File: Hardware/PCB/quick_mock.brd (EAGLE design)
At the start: 101.6 x 98.8 mm, 27 parts

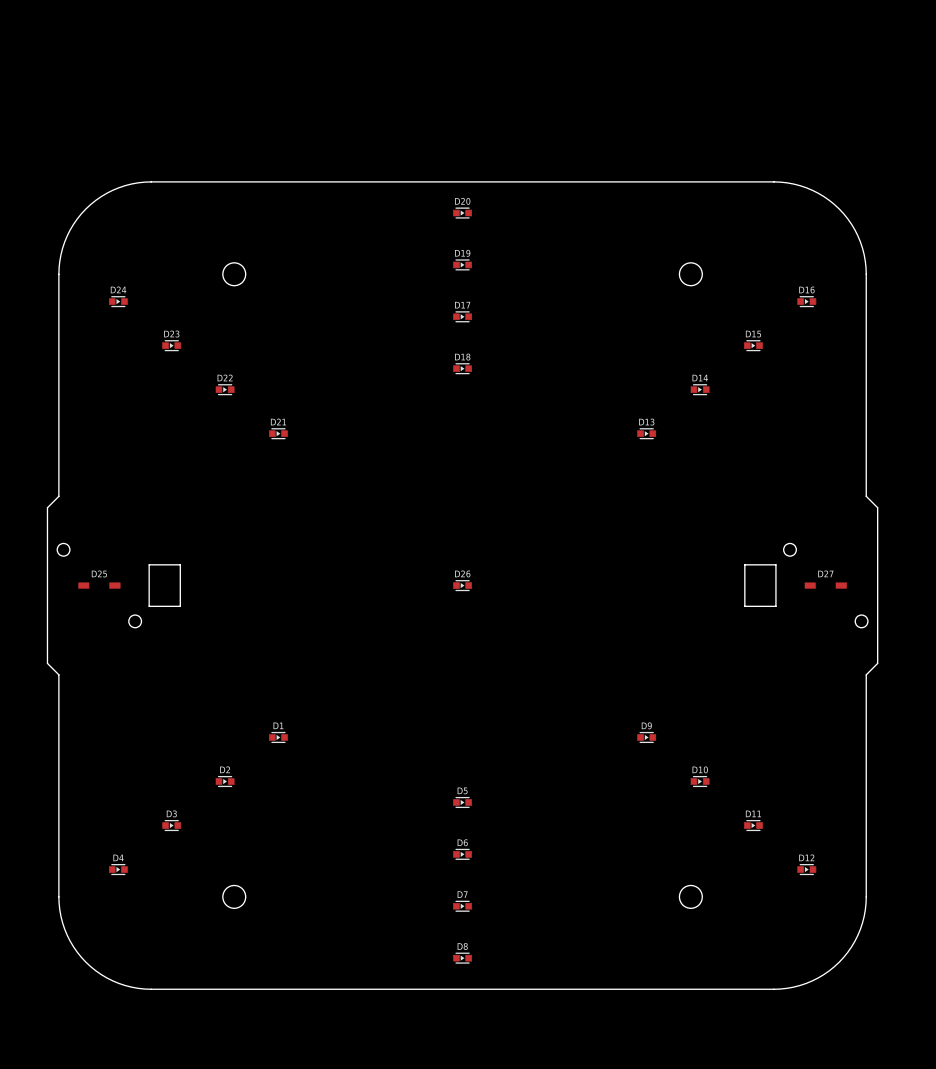
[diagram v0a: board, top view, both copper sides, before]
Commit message: move switches. add two types of lanyard mounting
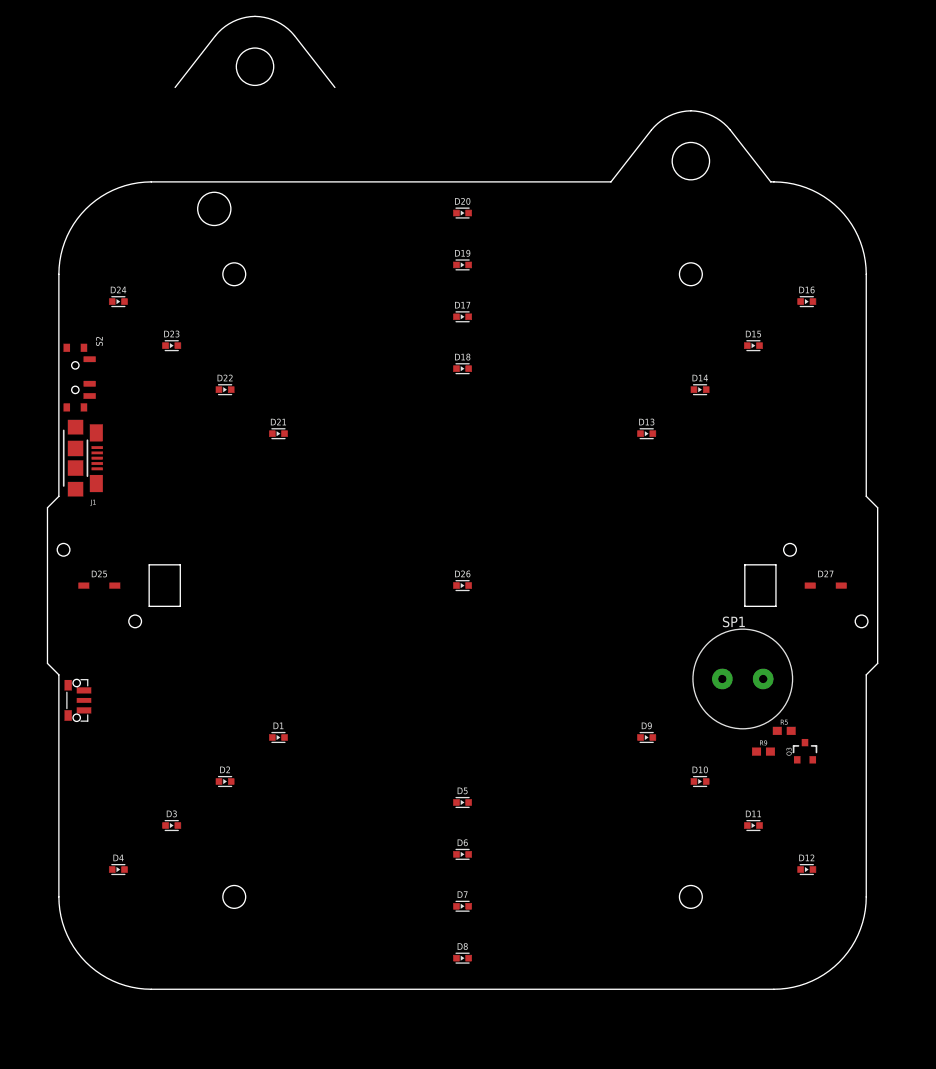
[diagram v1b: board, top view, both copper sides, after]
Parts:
- added J1: (no value), SparkFun-Connectors-new:USB-MICROB-10118192
- added Q3: 600mA/40V, SparkFun-DiscreteSemi:SOT23-3
- added R5, R9: 1k, SparkFun-Resistors:0603
- added S1: TL3340AF160QG, Rob-Switches:3PIN_GULLWING_4.0X3.3MM
- added S2: CUS-12B, IDEO-Switches:CUS-12_SPDT
- added SP1: SPEAKER/PS12, adafruit:PS12
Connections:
- new net 3.3V: R5.1, SP1.P$1
- new net BUZZER_OUT: R9.2
- new net GND: J1.GND, Q3.2
- new net N$26: Q3.1, R9.1
- new net N$3: Q3.3, R5.2, SP1.P$2
- new net VBUS: J1.VBUS
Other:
- board size 101.6 x 98.8 mm -> 101.6 x 119.1 mm
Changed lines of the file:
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@@
 <setting verticaltext="up"/>
 </settings>
-<grid distance="50" unitdist="mil" unit="mm" style="lines" multiple="1" display="yes" altdistance="5" altunitdist="mil" altunit="mil"/>
+<grid distance="50" unitdist="mil" unit="inch" style="lines" multiple="1" display="yes" altdistance="5" altunitdist="mil" altunit="mil"/>
 <layers>
 <layer number="1" name="Top" color="4" fill="1" visible="yes" active="yes"/>
@@
 <layer number="115" name="ReferenceISLANDS" color="7" fill="1" visible="no" active="yes"/>
 <layer number="116" name="Patch_BOT" color="9" fill="4" visible="no" active="yes"/>
+<layer number="117" name="art" color="7" fill="1" visible="yes" active="yes"/>
 <layer number="118" name="Rect_Pads" color="7" fill="1" visible="no" active="yes"/>
+<layer number="119" name="Bot_pads" color="1" fill="1" visible="yes" active="yes"/>
+<layer number="120" name="art2" color="7" fill="1" visible="yes" active="yes"/>
 <layer number="121" name="_tsilk" color="7" fill="1" visible="no" active="yes"/>
 <layer number="122" name="_bsilk" color="7" fill="1" visible="no" active="yes"/>
@@
 <layer number="128" name="_bValues" color="7" fill="1" visible="no" active="yes"/>
 <layer number="129" name="Mask" color="7" fill="1" visible="no" active="yes"/>
+<layer number="130" name="art3" color="7" fill="1" visible="yes" active="yes"/>
 <layer number="131" name="tAdjust" color="7" fill="1" visible="no" active="yes"/>
 <layer number="132" name="bAdjust" color="7" fill="1" visible="no" active="yes"/>
@@
 <layer number="230" name="230bmp" color="7" fill="1" visible="no" active="yes"/>
 <layer number="231" name="231bmp" color="7" fill="1" visible="no" active="yes"/>
+<layer number="232" name="Eagle3D_PG2" color="7" fill="1" visible="no" active="no"/>
+<layer number="233" name="Eagle3D_PG3" color="7" fill="1" visible="no" active="no"/>
 <layer number="248" name="Housing" color="7" fill="1" visible="no" active="yes"/>
 <layer number="249" name="Edge" color="7" fill="1" visible="no" active="yes"/>
@@
 </layers>
 <board>
-<fusionsync huburn="a.YnVzaW5lc3M6c3VuZGJlcmdmZXJhcg" projecturn="a.YnVzaW5lc3M6c3VuZGJlcmdmZXJhciMyMDIyMDkwNjU1MzEzMzI4MQ" f3durn="urn:adsk.wipprod:dm.lineage:_LBjbpjSReejQ1QNtJxQtQ" pcbguid="" lastpulledtime="" lastsyncedchangeguid="" latestrevisionid="c8c15753-8cb0-4c92-aaa7-c8cb3c30b25e" lastsyncedrevisionid="c8c15753-8cb0-4c92-aaa7-c8cb3c30b25e" lastboardhashguid="f6b63956-15fd-f67c-a3b4-4bf64a7ab889" lastpushedtime="2023-03-03T02:30:11Z" linktopcb3d="true"/>
+<fusionsync huburn="a.YnVzaW5lc3M6c3VuZGJlcmdmZXJhcg" projecturn="a.YnVzaW5lc3M6c3VuZGJlcmdmZXJhciMyMDIyMDkwNjU1MzEzMzI4MQ" f3durn="urn:adsk.wipprod:dm.lineage:_LBjbpjSReejQ1QNtJxQtQ" pcbguid="" lastpulledtime="" lastsyncedchangeguid="" latestrevisionid="f9e391af-d23a-44e8-a3fd-33513ed03db4" lastsyncedrevisionid="f9e391af-d23a-44e8-a3fd-33513ed03db4" lastboardhashguid="249d9e56-efed-2492-9fc4-1292afa326ac" lastpushedtime="2023-03-11T19:28:37Z" linktopcb3d="true"/>
 <plain>
 <wire x1="53.975" y1="24.695375" x2="53.88615625" y2="25.113003125" width="0" layer="49"/>
@@
 <circle x="12.7" y="12.7" radius="11.43" width="0.0254" layer="49"/>
 <wire x1="1.397" y1="88.9" x2="12.7" y2="100.203" width="0.0254" layer="20" curve="-90"/>
-<wire x1="12.7" y1="100.203" x2="88.9" y2="100.203" width="0.0254" layer="20"/>
 <wire x1="88.9" y1="100.203" x2="100.203" y2="88.9" width="0.0254" layer="20" curve="-90"/>
 <wire x1="100.203" y1="88.9" x2="100.203" y2="61.722" width="0.0254" layer="20"/>
@@
 <text x="97.79" y="57.15" size="1.778" layer="51" font="vector">Transmitter</text>
 <polygon width="0.1" layer="39">
-<vertex x="1.27" y="64.262"/>
-<vertex x="1.27" y="62.865"/>
-<vertex x="2.54" y="62.23"/>
-<vertex x="2.54" y="63.754"/>
-<vertex x="1.27" y="64.389"/>
-</polygon>
-<polygon width="0.1" layer="39">
-<vertex x="1.27" y="37.338"/>
-<vertex x="1.27" y="38.735"/>
-<vertex x="2.54" y="39.37"/>
-<vertex x="2.54" y="37.846"/>
-<vertex x="1.27" y="37.211"/>
-</polygon>
-<polygon width="0.1" layer="39">
 <vertex x="100.33" y="62.865"/>
 <vertex x="100.33" y="64.389"/>
@@
 <vertex x="2.54" y="82.55"/>
 </polygon>
+<hole x="20.414" y="96.901" drill="4.064"/>
+<hole x="78.74" y="102.743" drill="4.572"/>
+<wire x1="78.74" y1="108.9025" x2="73.914" y2="106.553" width="0.0254" layer="20" curve="50"/>
+<wire x1="73.914" y1="106.553" x2="68.961" y2="100.203" width="0.0254" layer="20"/>
+<wire x1="78.74" y1="108.9025" x2="83.566" y2="106.553" width="0.0254" layer="20" curve="-50"/>
+<wire x1="83.566" y1="106.553" x2="88.519" y2="100.203" width="0.0254" layer="20"/>
+<hole x="25.4" y="114.3" drill="4.572"/>
+<wire x1="25.4" y1="120.4595" x2="20.574" y2="118.11" width="0.01" layer="20" curve="50"/>
+<wire x1="20.574" y1="118.11" x2="15.621" y2="111.76" width="0.01" layer="20"/>
+<wire x1="25.4" y1="120.4595" x2="30.226" y2="118.11" width="0.01" layer="20" curve="-50"/>
+<wire x1="30.226" y1="118.11" x2="35.179" y2="111.76" width="0.01" layer="20"/>
+<wire x1="88.9" y1="100.203" x2="88.519" y2="100.203" width="0.0254" layer="20"/>
+<wire x1="68.961" y1="100.203" x2="12.7" y2="100.203" width="0.0254" layer="20"/>
 </plain>
 <attributes>
@@
 <attribute name="VALUE" x="95.25" y="49.784" size="0.8128" layer="27" font="vector" ratio="12" align="top-center"/>
 </element>
+<element name="S2" library="IDEO-Switches" package="CUS-12_SPDT" override_package3d_urn="urn:adsk.eagle:package:39505090/2" override_package_urn="urn:adsk.eagle:footprint:39505091/1" value="CUS-12B" x="3.41" y="76.25" smashed="yes" rot="R270">
+<attribute name="NAME" x="5.95" y="80.06" size="0.8128" layer="25" ratio="15" rot="R270" align="bottom-right"/>
+</element>
+<element name="J1" library="SparkFun-Connectors-new" package="USB-MICROB-10118192" override_package3d_urn="urn:adsk.eagle:package:39505002/4" override_package_urn="urn:adsk.eagle:footprint:39505003/1" value="" x="3.44" y="66.39" smashed="yes" rot="R270">
+<attribute name="NAME" x="5.98" y="61.31" size="0.6096" layer="25" font="vector" ratio="20" rot="R180"/>
+<attribute name="VALUE" x="5.345" y="71.47" size="0.6096" layer="27" font="vector" ratio="20" rot="R180" align="top-left"/>
+</element>
+<element name="S1" library="Rob-Switches" library_urn="urn:adsk.eagle:library:39524603" package="3PIN_GULLWING_4.0X3.3MM" package3d_urn="urn:adsk.eagle:package:39524606/4" value="TL3340AF160QG" x="2.076" y="36.75" smashed="yes" rot="R270"/>
+<element name="Q3" library="SparkFun-DiscreteSemi" package="SOT23-3" value="600mA/40V" x="92.71" y="30.48" smashed="yes">
+<attribute name="NAME" x="91.059" y="30.48" size="0.6096" layer="25" font="vector" ratio="20" rot="R90" align="bottom-center"/>
+<attribute name="PROD_ID" value="TRANS-08049" x="92.71" y="45.72" size="1.778" layer="27" display="off"/>
+<attribute name="VALUE" x="94.361" y="30.48" size="0.6096" layer="27" font="vector" ratio="20" rot="R90" align="top-center"/>
+</element>
+<element name="R9" library="SparkFun-Resistors" package="0603" value="1k" x="87.63" y="30.48" smashed="yes">
+<attribute name="NAME" x="87.63" y="31.242" size="0.6096" layer="25" font="vector" ratio="20" align="bottom-center"/>
+<attribute name="PROD_ID" value="RES-00824" x="77.47" y="40.64" size="1.778" layer="27" display="off"/>
+<attribute name="VALUE" x="87.63" y="29.718" size="0.6096" layer="27" font="vector" ratio="20" align="top-center"/>
+</element>
+<element name="R5" library="SparkFun-Resistors" package="0603" value="1k" x="90.17" y="33.02" smashed="yes">
+<attribute name="NAME" x="90.17" y="33.782" size="0.6096" layer="25" font="vector" ratio="20" align="bottom-center"/>
+<attribute name="PROD_ID" value="RES-00824" x="83.82" y="39.37" size="1.778" layer="27" display="off"/>
+<attribute name="VALUE" x="90.17" y="32.258" size="0.6096" layer="27" font="vector" ratio="20" align="top-center"/>
+</element>
+<element name="SP1" library="adafruit" package="PS12" override_package3d_urn="urn:adsk.eagle:package:39544791/3" override_package_urn="urn:adsk.eagle:footprint:39544792/1" value="SPEAKER/PS12" x="85.09" y="39.37" smashed="yes">
+<attribute name="NAME" x="82.55" y="45.72" size="1.27" layer="25" ratio="10"/>
+<attribute name="VALUE" x="81.2038" y="35.56" size="1.27" layer="27" ratio="10"/>
+</element>
 </elements>
 <signals>
+<signal name="VBUS">
+<contactref element="J1" pad="VBUS"/>
+</signal>
+<signal name="GND">
+<contactref element="J1" pad="GND"/>
+<contactref element="Q3" pad="2"/>
+<wire x1="93.66" y1="29.48" x2="6.09" y2="65.09" width="0" layer="19" extent="1-1"/>
+</signal>
+<signal name="3.3V">
+<contactref element="R5" pad="1"/>
+<contactref element="SP1" pad="P$1"/>
+<wire x1="89.32" y1="33.02" x2="82.59" y2="39.37" width="0" layer="19" extent="1-1"/>
+</signal>
+<signal name="BUZZER_OUT">
+<contactref element="R9" pad="2"/>
+</signal>
+<signal name="N$26">
+<contactref element="R9" pad="1"/>
+<contactref element="Q3" pad="1"/>
+<wire x1="86.78" y1="30.48" x2="91.76" y2="29.48" width="0" layer="19" extent="1-1"/>
+</signal>
+<signal name="N$3">
+<contactref element="R5" pad="2"/>
+<contactref element="Q3" pad="3"/>
+<contactref element="SP1" pad="P$2"/>
+<wire x1="91.02" y1="33.02" x2="87.59" y2="39.37" width="0" layer="19" extent="1-1"/>
+<wire x1="92.71" y1="31.58" x2="91.02" y2="33.02" width="0" layer="19" extent="1-1"/>
+</signal>
 </signals>
 <mfgpreviewcolors>
@@
 packages will not be understood (or retained) with this version.
 </note>
+<note version="9.4" severity="warning">
+Since Version 9.4, EAGLE supports the overriding of 3D packages
+in schematics and board files. Those overridden 3d packages
+will not be understood (or retained) with this version.
+</note>
 </compatibility>

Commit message: adjust lanyard holes. prep mock PCB for fab.
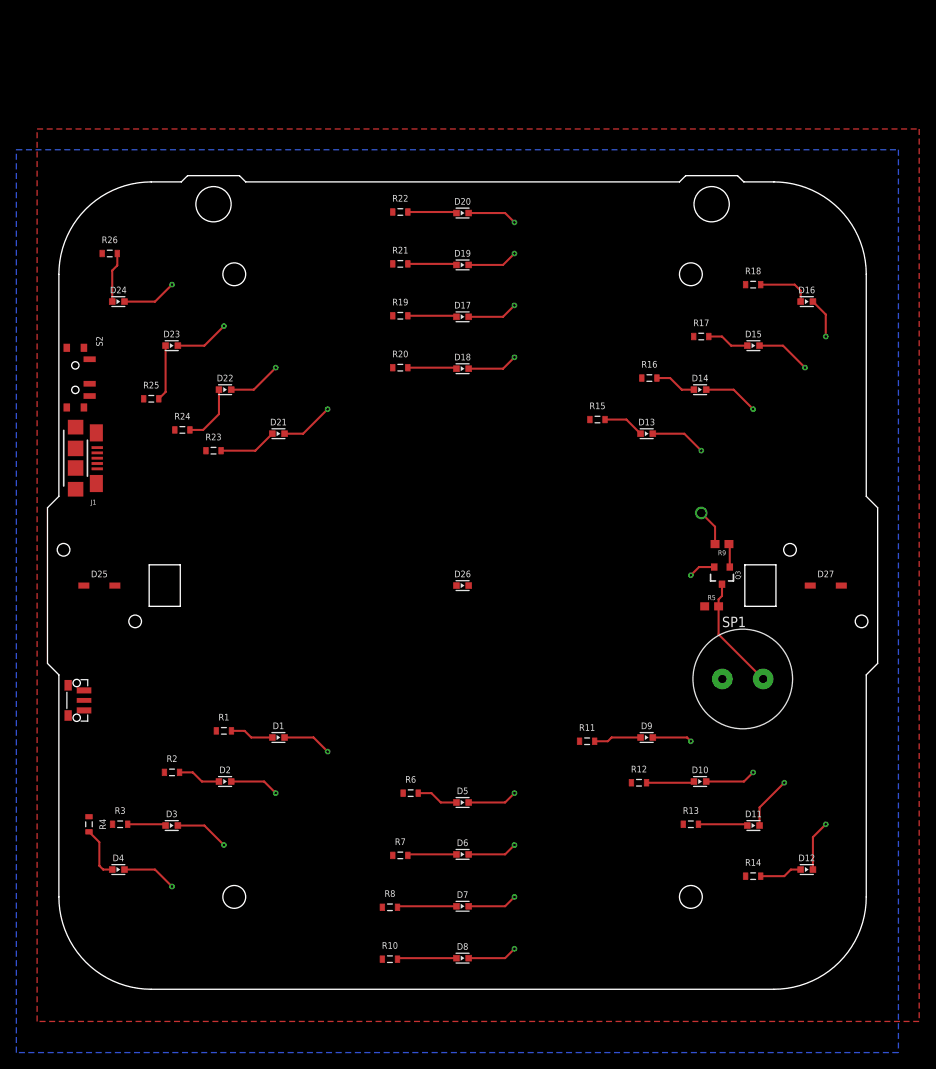
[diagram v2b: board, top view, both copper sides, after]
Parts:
- added R1, R10, R11, R12, R13, R14, R15, R16, R17, R18, R19, R2, R20, R21, R22, R23, R24, R25, R26, R3, R4, R6, R7, R8: (no value), Rob-Resistors:SMD-603
- moved R9 25.9 mm to (82.5, 55.9), turned to 180 degrees
- moved Q3 23.9 mm to (82.5, 52.1), turned to 180 degrees
- moved R5 17.6 mm to (81.3, 48.3)
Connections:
- new net N$1: D1.P$1, R1.2
- new net N$14: D9.P$1, R11.2
- new net N$15: D10.P$1, R12.2
- new net N$16: D11.P$1, R13.2
- new net N$17: D12.P$1, R14.2
- new net N$18: D13.P$1, R15.2
- new net N$19: D14.P$1, R16.2
- new net N$2: D2.P$1, R2.2
- new net N$20: D15.P$1, R17.2
- new net N$21: D16.P$1, R18.2
- new net N$22: D24.P$1, R26.2
- new net N$23: D23.P$1, R25.2
- new net N$24: D22.P$1, R24.2
- new net N$25: D21.P$1, R23.2
- new net N$27: D20.P$1, R22.2
- new net N$28: D19.P$1, R21.2
- new net N$29: D18.P$1, R20.2
- new net N$30: D17.P$1, R19.2
- new net N$4: D3.P$1, R3.2
- new net N$5: D4.P$1, R4.2
- new net N$6: D5.P$1, R6.2
- new net N$7: D6.P$1, R7.2
- new net N$8: D7.P$1, R8.2
- new net N$9: D8.P$1, R10.2
- net 3.3V: now also R1.1, R10.1, R11.1, R12.1, R13.1, R14.1, R15.1, R16.1, R17.1, R18.1, R19.1, R2.1, R20.1, R21.1, R22.1, R23.1, R24.1, R25.1, R26.1, R3.1, R4.1, R6.1, R7.1, R8.1
- net GND: now also D1.P$2, D10.P$2, D11.P$2, D12.P$2, D13.P$2, D14.P$2, D15.P$2, D16.P$2, D17.P$2, D18.P$2, D19.P$2, D2.P$2, D20.P$2, D21.P$2, D22.P$2, D23.P$2, D24.P$2, D3.P$2, D4.P$2, D5.P$2, D6.P$2, D7.P$2, D8.P$2, D9.P$2
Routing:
- net GND: track 0.00 -> 152.8 mm, vias 0 -> 25
- net N$3: track 0.00 -> 14.0 mm
- net N$24: track 0.00 -> 7.34 mm
- net N$8: track 0.00 -> 7.27 mm
- net N$9: track 0.00 -> 7.27 mm
- net N$25: track 0.00 -> 7.13 mm
- net N$23: track 0.00 -> 6.85 mm
- net N$21: track 0.00 -> 6.54 mm
- net N$5: track 0.00 -> 6.45 mm
- net N$22: track 0.00 -> 6.14 mm
- net N$16: track 0.00 -> 6.04 mm
- net N$7: track 0.00 -> 6.00 mm
- net N$30: track 0.00 -> 6.00 mm
- net N$29: track 0.00 -> 6.00 mm
- net N$28: track 0.00 -> 6.00 mm
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- added copper zone on layer 1, net 3.3V
- added copper zone on layer 16, net GND
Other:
- board size 101.6 x 119.1 mm -> 101.6 x 99.6 mm
